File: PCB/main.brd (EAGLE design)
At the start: 80 x 50 mm, 53 parts, among them J1 DC-005, J4 4p-2.54, Q1 CSD17578Q3A

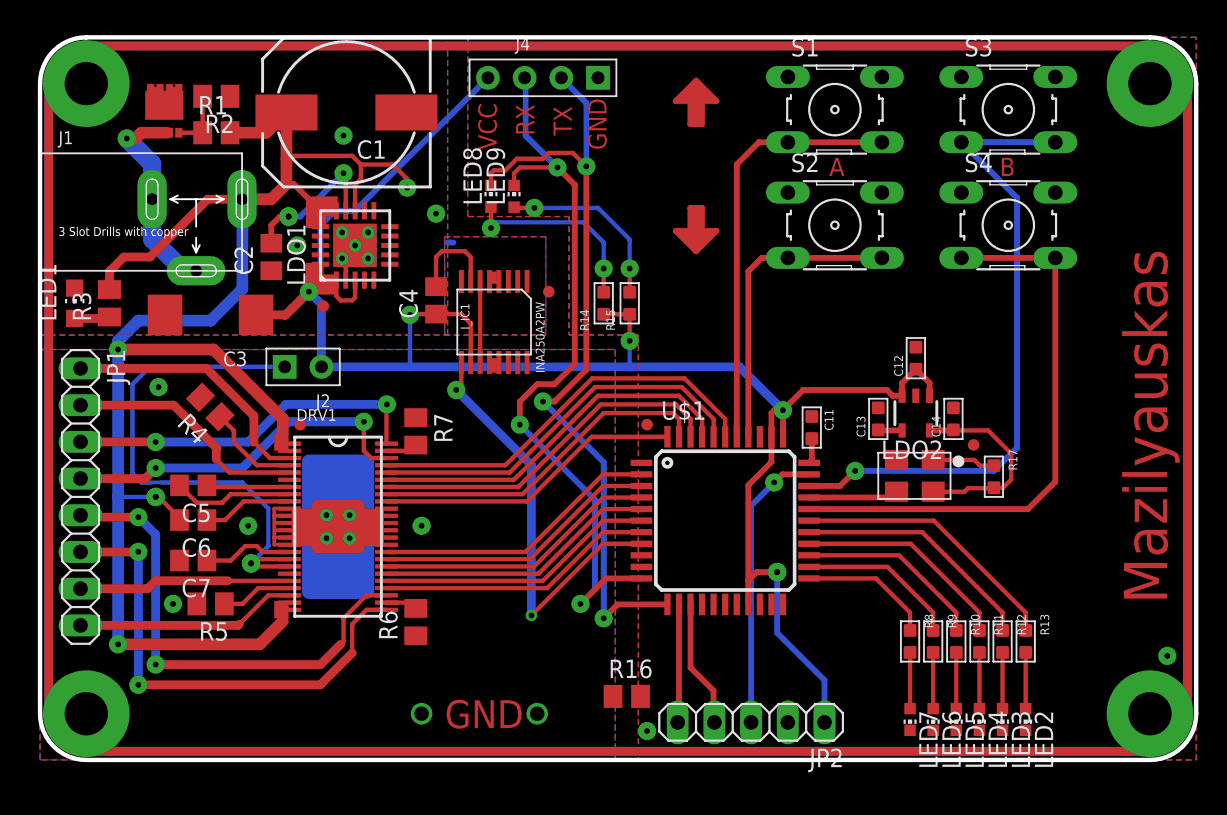
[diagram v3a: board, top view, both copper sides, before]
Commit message: Change Power Regulator
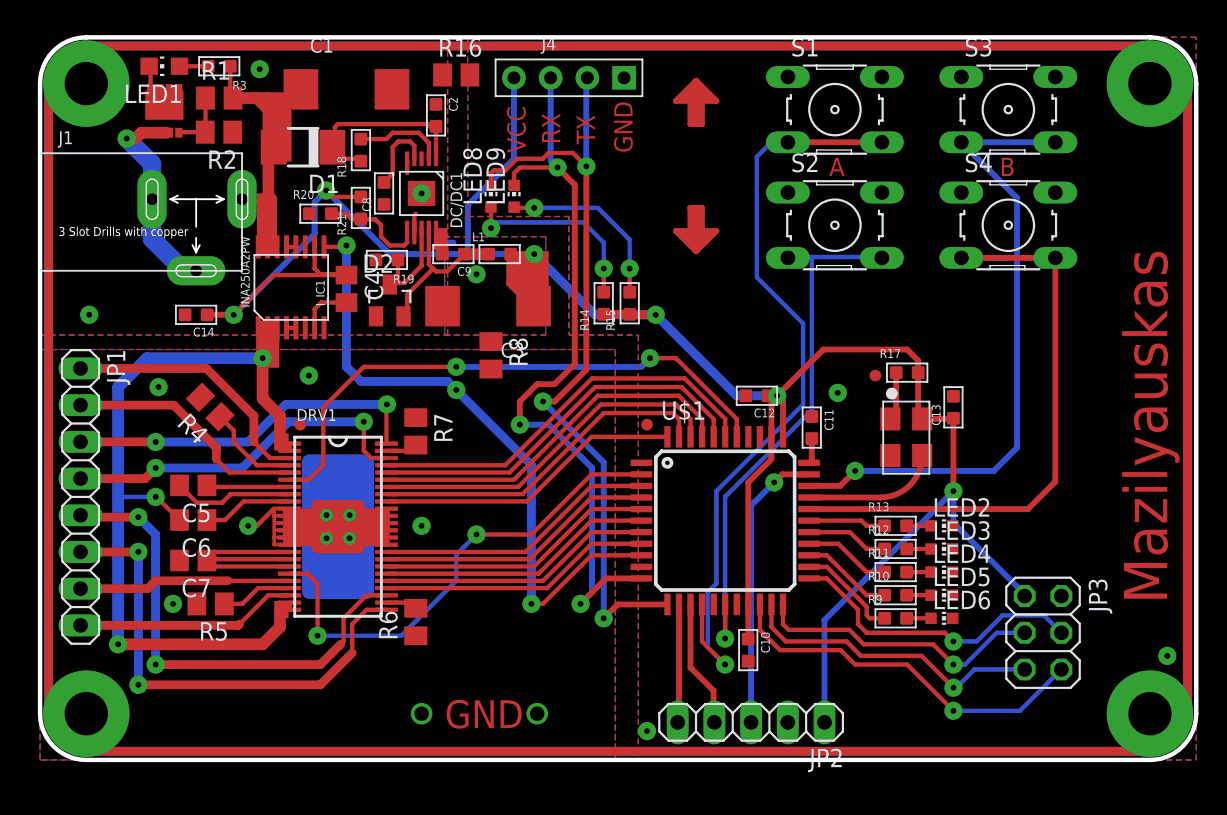
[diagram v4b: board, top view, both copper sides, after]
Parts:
- removed J2: (no value), Seeed-OPL-Connector:H2-2.54
- removed LDO1: TPS7A470X, My_TI:QFN20
- removed LDO2: TPS736, My_TI:SOT23-5
- removed LED7: (no value), led:CHIP-LED0603
- added C10, C8, C9: (no value), My_RLC:C0603
- added D1: (no value), diode:DO-214AC
- added D2: (no value), diode:SOT23
- added DC/DC1: (no value), My_TI:HVSSOP-10
- added JP3: (no value), pinhead:2X03
- added L1: (no value), My_RLC:L0603
- added R18, R19, R20, R21: (no value), My_RLC:R0603
- C1: device rcl:150CLZ-1010 -> rcl:SMC_D
- C2: device rcl:C0805 -> My_RLC:C0603
- R3: device rcl:M0805 -> My_RLC:R0603
- R8: device My_RLC:R0603 -> rcl:M0805
- moved C14 52.9 mm to (10.8, 30.8), turned to 270 degrees
- moved R16 44.6 mm to (28.8, 47.4)
- moved R8 35.1 mm to (31.2, 28.0), turned to 270 degrees
- moved C3 19.2 mm to (31.0, 31.4)
- moved R3 18.1 mm to (12.4, 48.0)
- moved LED1 17.5 mm to (8.60, 48.0), turned to 90 degrees
- moved C2 15.0 mm to (27.4, 44.6), turned to 0 degrees
- moved LED2 14.6 mm to (62.4, 16.2), turned to 270 degrees
- moved I_IC1 14.2 mm to (17.4, 32.8), turned to 0 degrees
- moved LED3 12.5 mm to (62.4, 14.6), turned to 270 degrees
- moved R13 12.0 mm to (59.2, 16.2), turned to 270 degrees
- moved C12 11.3 mm to (49.6, 25.2), turned to 270 degrees
- moved LED4 10.5 mm to (62.4, 13.0), turned to 270 degrees
- moved R12 9.78 mm to (59.2, 14.6), turned to 270 degrees
- moved R17 9.37 mm to (60.0, 26.8), turned to 270 degrees
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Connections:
- removed net +5V: C12.1, C3.+, C4.1, I_IC1.P$10, J2.2, J4.4, JP2.1, LDO1.1, LDO1.20, LDO1.3, LDO2.1, LDO2.3, R14.2, R15.2, U$1.19, U$1.34, U$1.35
- removed net N$34: S1.3, S1.4, U$1.38
- removed net N$35: S2.3, S2.4, U$1.37
- new net ABDECACY: DRV1.6, U$1.38
- new net BUT1: S1.3, S1.4, U$1.15
- new net BUT2: S2.3, S2.4, U$1.17
- new net CDDECACY: DRV1.19, U$1.2
- new net N$20: JP3.4, U$1.23
- new net N$26: DC/DC1.2, R18.1
- new net N$5: C8.2, DC/DC1.4
- new net N$51: C9.2, DC/DC1.10
- new net N$52: C9.1, D2.2, DC/DC1.9, L1.1
- new net N$60: DC/DC1.6, R20.1, R21.2
- new net VCC: C6.2, DRV1.1, DRV1.2, DRV1.23, DRV1.24, I_IC1.P$1, I_IC1.P$2, I_IC1.P$3
- net +24V: now also D1.A, I_IC1.P$14, I_IC1.P$15, I_IC1.P$16; no longer C6.2, DRV1.1, DRV1.2, DRV1.23, DRV1.24, LDO1.13, LDO1.15, LDO1.16
- net +3V3: now also C10.1, C12.1, C13.1, C3.+, C4.1, I_IC1.P$10, J4.4, JP2.1, JP3.1, L1.2, R14.2, R15.2, R21.1, U$1.19, U$1.34, U$1.35; no longer LDO2.5
- net AGND: now also C14.2, C8.1, DC/DC1.5, DC/DC1.7, DC/DC1.EPAD, R16.1, R19.1, R20.2, R8.1; no longer I_IC1.P$1, I_IC1.P$2, I_IC1.P$3, I_IC1.P$6, LDO1.11, LDO1.12, LDO1.2, LDO1.6, LDO1.7, LDO1.8, LDO1.EPAD_BUTTOM, LDO1.EPAD_TOP, LDO1.EPAD_VIA1, LDO1.EPAD_VIA2, LDO1.EPAD_VIA3, LDO1.EPAD_VIA4, LDO1.EPAD_VIA5
- net CDDIR: now also U$1.5; no longer U$1.4
- net CDENBLN: now also U$1.6; no longer U$1.5
- net CDRESETN: now also U$1.8; no longer U$1.7
- net CDSTEP: now also U$1.3; no longer U$1.2
- net CDUSM0: now also U$1.4; no longer U$1.3
- net CDUSM1: now also U$1.7; no longer U$1.6
- net CURRENT: now also U$1.9; no longer U$1.8
- net GND: now also C10.2, JP3.2; no longer C14.2, LDO2.2, LED7.C
- net GNDA: now also R8.2; no longer I_IC1.P$14, I_IC1.P$15, I_IC1.P$16, R16.1
- net N$2: now also D1.C, DC/DC1.1, R18.2; no longer LDO1.14
- net N$25: now also JP3.3, U$1.22; no longer C7.1, DRV1.16
- net N$27: now also C7.1, DRV1.16; no longer J2.1
- net N$33: now also JP3.5, U$1.21; no longer R8.2, U$1.23
- net N$38: now also JP3.6, U$1.20; no longer LED7.A, R8.1
- net N$57: now also D2.3, DC/DC1.8, R19.2; no longer C13.1, LDO2.4
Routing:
- net +3V3: track 15.9 -> 161.7 mm, vias 0 -> 6
- net +5V: track 133.6 -> 0.00 mm, vias 5 -> 0
- net +24V: track 117.3 -> 21.3 mm, vias 4 -> 0
- net VCC: track 0.00 -> 61.6 mm, vias 0 -> 3
- net BUT1: track 0.00 -> 53.6 mm, vias 0 -> 1
- net ABDECACY: track 0.00 -> 39.7 mm, vias 0 -> 2
- net BUT2: track 0.00 -> 37.8 mm, vias 0 -> 1
- net CDDECACY: track 0.00 -> 33.9 mm, vias 0 -> 2
- net N$34: track 29.5 -> 0.00 mm
- net N$38: track 3.89 -> 26.1 mm, vias 0 -> 1
- net N$20: track 0.00 -> 21.1 mm
- net N$35: track 21.1 -> 0.00 mm
- net N$27: track 37.5 -> 18.2 mm, vias 1 -> 0
- net CURRENT: track 29.5 -> 44.7 mm, vias 2 -> 3
- net N$28: track 18.9 -> 5.38 mm
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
